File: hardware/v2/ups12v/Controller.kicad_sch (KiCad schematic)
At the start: 0 parts

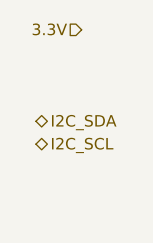
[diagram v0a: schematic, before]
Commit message: add power output to the J4
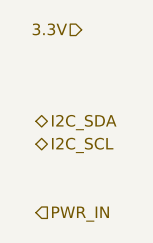
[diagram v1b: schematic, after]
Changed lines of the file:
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@@
+		)
+	)
+	(hierarchical_label "PWR_IN"
+		(shape input)
+		(at 45.72 66.04 0)
+		(fields_autoplaced yes)
+		(effects
+			(font
+				(size 1.27 1.27)
+			)
+			(justify left)
 		)
 	)

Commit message: temporary changes to PCB and schematics
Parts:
- added J5: Conn_01x04_Pin, symbol Connector:Conn_01x04_Pin
- added U1: mini_esp32 MH-ET-Live, Modules_MCU:ESP32_mini MH-ET-LIVE, symbol My Modules_MCU:mini_esp32
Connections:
- net I2C_SCL: now also U1.25 (IO_22/D1/SCL)
- net I2C_SDA: now also U1.27 (IO_21/D2/SDA)
- net PWR_IN: now also J5.2 (IN)
- new net: J5.4 (OUT), U1.16 (3V3)
- new net GND: J5.3 (GND), U1.1 (GND), U1.22 (GND), U1.33 (GND)
- no-connect marks 0 -> 12
